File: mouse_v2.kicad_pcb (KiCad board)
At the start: 2 copper layers, 46.4 x 63 mm, 110 parts, among them J1 DEBUGGER, J10 ENC_MASTER, J11 ENC_SLAVE, J12 MOTOR1, J13 MOTOR2, J14 BATT, J15 DEBUGGER_CONN, J16 JLink_Conn, J2 TOF_MASTER, J3 TOF_SLAVE, J4 TOF_MASTER, J5 TOF_SLAVE, J6 TOF_MASTER, J7 TOF_SLAVE, J8 ENC_MASTER, J9 ENC_SLAVE, Q1 IRFML8244, Q2 IRLML6402, Q3 IRFML8244, Q4 IRFML8244, SW1 RESET_SW, SW2 BATTERY_SW, SW3 USER_SW, U1 STM32F413C, U10 AD8602D, U11 TPS62203DBV, U12 TPS62200DBV, U2 VL6180X, U3 VL6180X, U4 VL6180X, U5 MA702GQ, U6 MA702GQ, U7 DRV8835, U8 ICM20648, U9 NJM2732

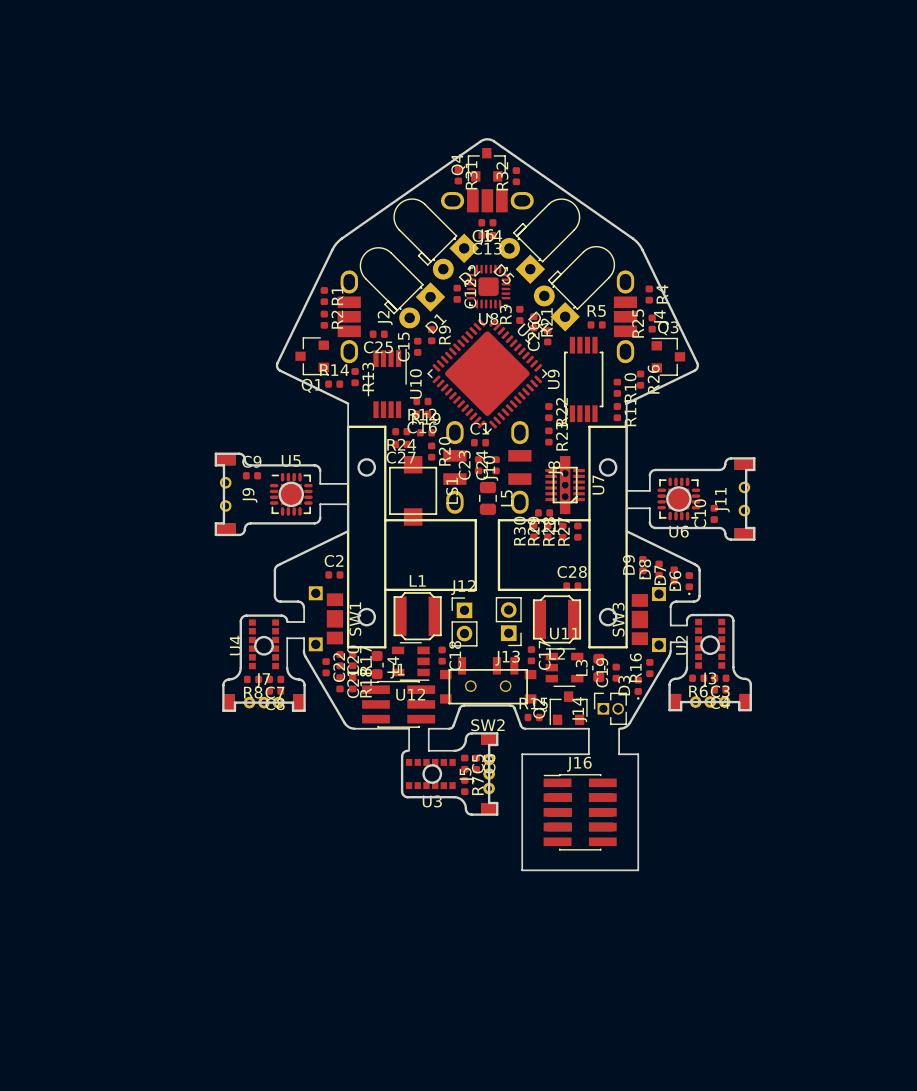
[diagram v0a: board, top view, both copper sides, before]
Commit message: [add] Finished to manual routing.
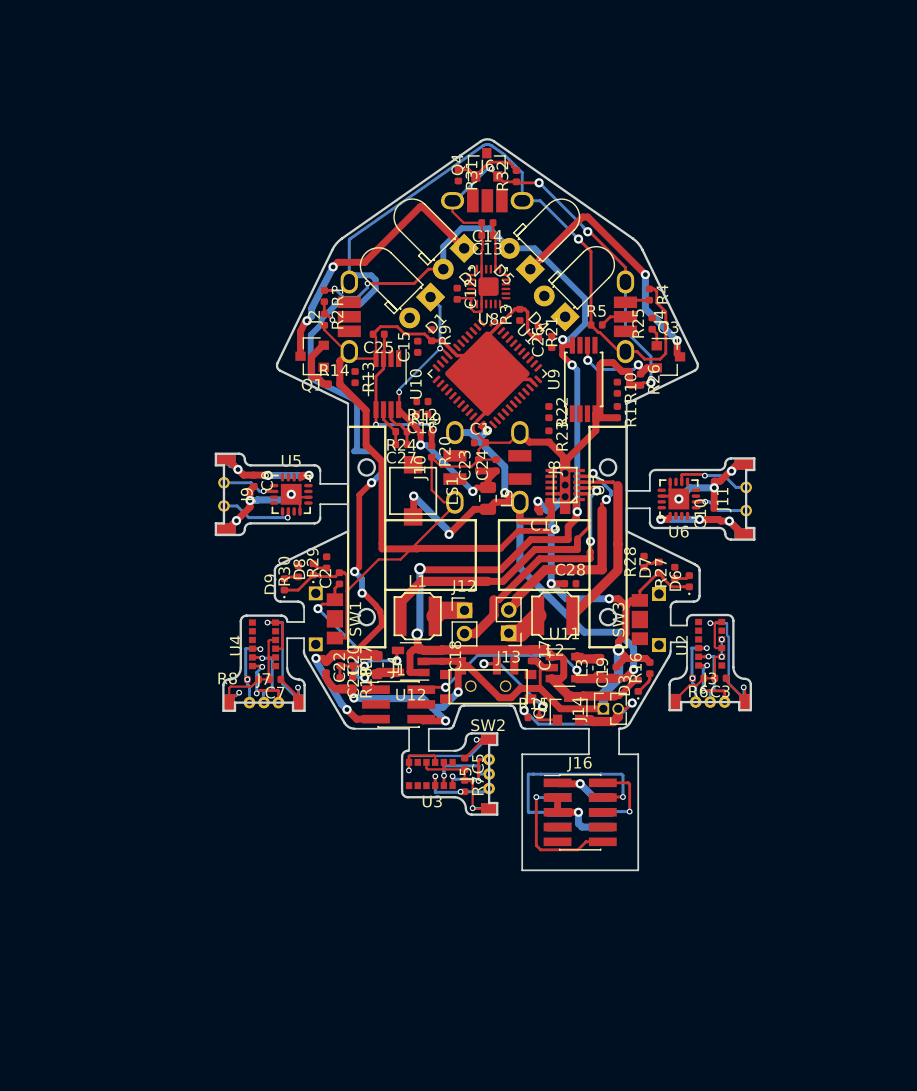
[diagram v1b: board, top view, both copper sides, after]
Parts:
- removed C4, C6, C8: 100n, Capacitor_SMD:C_0402_1005Metric
- moved D9 30.9 mm to (133.8, 119.7)
- moved D8 29.8 mm to (136.3, 118.4)
- moved R30 20.6 mm to (135.0, 118.5)
- moved R29 19.2 mm to (137.4, 117.8)
- moved R27 9.07 mm to (167.4, 118.7)
- moved R28 7.47 mm to (164.8, 117.7)
- moved D7 1.46 mm to (166.1, 118.2)
- moved R21 0.92 mm to (155.7, 97.9)
- moved C26 0.59 mm to (156.8, 98.8)
- moved C2 0.52 mm to (138.5, 119.1), turned to 90 degrees
- moved C9 0.46 mm to (131.2, 110.7), turned to 270 degrees
- moved L2 0.36 mm to (157.1, 122.4)
- moved C28 0.26 mm to (158.4, 119.6)
- moved C11 0.16 mm to (156.3, 113.4)
- moved J11 0.15 mm to (173.6, 112.3)
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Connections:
- net Net-(J15-Pad2) renamed /converter/3.3V
- net Net-(J15-Pad6) renamed /converter/t_GND
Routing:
- net GND: track 0.00 -> 275.3 mm, vias 0 -> 12
- net 2.8V: track 0.00 -> 112.5 mm, vias 0 -> 6
- net BATT: track 0.00 -> 103.0 mm, vias 0 -> 7
- net 3.3V: track 0.00 -> 76.2 mm, vias 0 -> 7
- net 3.3VA: track 0.00 -> 27.2 mm, vias 0 -> 4
- net Net-(L1-Pad2): track 0.00 -> 24.6 mm
- net Net-(D2-Pad1): track 0.00 -> 23.5 mm, vias 0 -> 2
- net Net-(J12-Pad2): track 0.00 -> 22.2 mm, vias 0 -> 2
- net Net-(D5-Pad1): track 0.00 -> 22.2 mm, vias 0 -> 2
- net Net-(J13-Pad2): track 0.00 -> 20.5 mm, vias 0 -> 2
- net /converter/SWCLK: track 0.00 -> 18.5 mm, vias 0 -> 1
- net /ToF3/t_GND: track 0.00 -> 18.3 mm, vias 0 -> 2
- net /ToF1/t_GND: track 0.00 -> 18.0 mm, vias 0 -> 2
- net /ToF2/t_GND: track 0.00 -> 17.8 mm, vias 0 -> 2
- net Net-(J14-Pad2): track 0.00 -> 17.0 mm, vias 0 -> 2
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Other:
- outline, holes or cut-outs redrawn
- net class Default: via_dia 0.8 -> 0.5; via_drill 0.4 -> 0.3
- net class Power added: clearance 0.2, trace_width 0.6, via_dia 0.8, via_drill 0.4

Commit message: [add] Completed routing.
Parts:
- removed D9: LED4, LED_SMD:LED_0402_1005Metric
- removed R30: 1k, Resistor_SMD:R_0402_1005Metric
- moved D6 31.9 mm to (136.8, 118.0)
- moved D7 30.7 mm to (135.4, 118.7)
- moved R28 21.8 mm to (143.2, 114.8)
- moved R27 16.7 mm to (151.1, 115.2)
- moved D8 2.47 mm to (134.0, 119.4)
- moved R29 1.49 mm to (138.6, 116.8)
- moved R9 0.40 mm to (146.4, 98.6)
- moved R12 0.19 mm to (145.5, 103.9)
- moved R21 0.10 mm to (155.8, 97.9)
- renumbered SW2 to ?, J16 to ?, SW1 to ?, U2 to ?, U3 to ?, U4 to ?, U5 to ?, U6 to ?, U8 to ?, J2 to ?, J4 to ?, SW3 to ?, J6 to ?, J8 to ?, J10 to ?, J9 to ?, J11 to ?, U1 to ?, J3 to ?, J5 to ?, J7 to ?, J12 to ?, J13 to ?, J15 to ?
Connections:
- ? pad 10: /MCU/ENC1_A -> /MCU/ENC1_B
- ? pad 11: /MCU/ENC1_B -> /MCU/ENC1_A
- ? pad 18: /MCU/LED1 -> Net-(U1-Pad18)
- ? pad 20: /MCU/LED3 -> Net-(U1-Pad20)
- ? pad 21: /MCU/LED4 -> Net-(U1-Pad21)
- ? pad 25: /MCU/TOF3_EN -> /MCU/LED1
- ? pad 26: /MCU/TOF2_EN -> /MCU/LED3
- ? pad 27: /MCU/TOF1_EN -> Net-(U1-Pad27)
- ? pad 38: /MCU/IMU_NSS -> /MCU/TOF2_EN
- ? pad 4: Net-(U1-Pad4) -> /MCU/IMU_NSS
- ? pad 43: Net-(U1-Pad43) -> /MCU/TOF3_EN
- ? pad 6: Net-(U1-Pad6) -> /MCU/TOF1_EN
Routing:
- net /MCU/SWDIO: track 0.00 -> 57.4 mm, vias 0 -> 4
- net /MCU/SWCLK: track 0.00 -> 54.1 mm, vias 0 -> 4
- net /MCU/TOF_SDA: track 2.12 -> 55.8 mm, vias 0 -> 9
- net Net-(C26-Pad1): track 3.43 -> 55.7 mm, vias 0 -> 6
- net /MCU/TOF_SCL: track 2.29 -> 50.1 mm, vias 0 -> 5
- net 3.3V: track 76.2 -> 111.0 mm, vias 7 -> 12
- net /MCU/BUTTON: track 0.00 -> 34.7 mm, vias 0 -> 10
- net Net-(LS1-Pad2): track 0.00 -> 33.5 mm, vias 0 -> 4
- net /MCU/NRST: track 12.7 -> 46.1 mm, vias 2 -> 6
- net Net-(R13-Pad2): track 0.00 -> 32.7 mm, vias 0 -> 4
- net Net-(Q1-Pad2): track 4.84 -> 37.2 mm, vias 0 -> 8
- net /MCU/LED3: track 0.00 -> 30.2 mm, vias 0 -> 2
- net /MCU/SPEAKER: track 0.00 -> 26.3 mm, vias 0 -> 6
- net /MCU/TOF3_EN: track 0.00 -> 21.3 mm, vias 0 -> 6
- net /MCU/TOF1_EN: track 0.00 -> 16.5 mm, vias 0 -> 4
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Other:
- net class Default: clearance 0.2 -> 0.14; trace_width 0.25 -> 0.2; via_dia 0.5 -> 0.4
- net class Power: clearance 0.2 -> 0.14; via_dia 0.8 -> 0.4; via_drill 0.4 -> 0.3
- rule trace_clearance: 0.2 -> 0.14
- rule trace_min: 0.2 -> 0.152

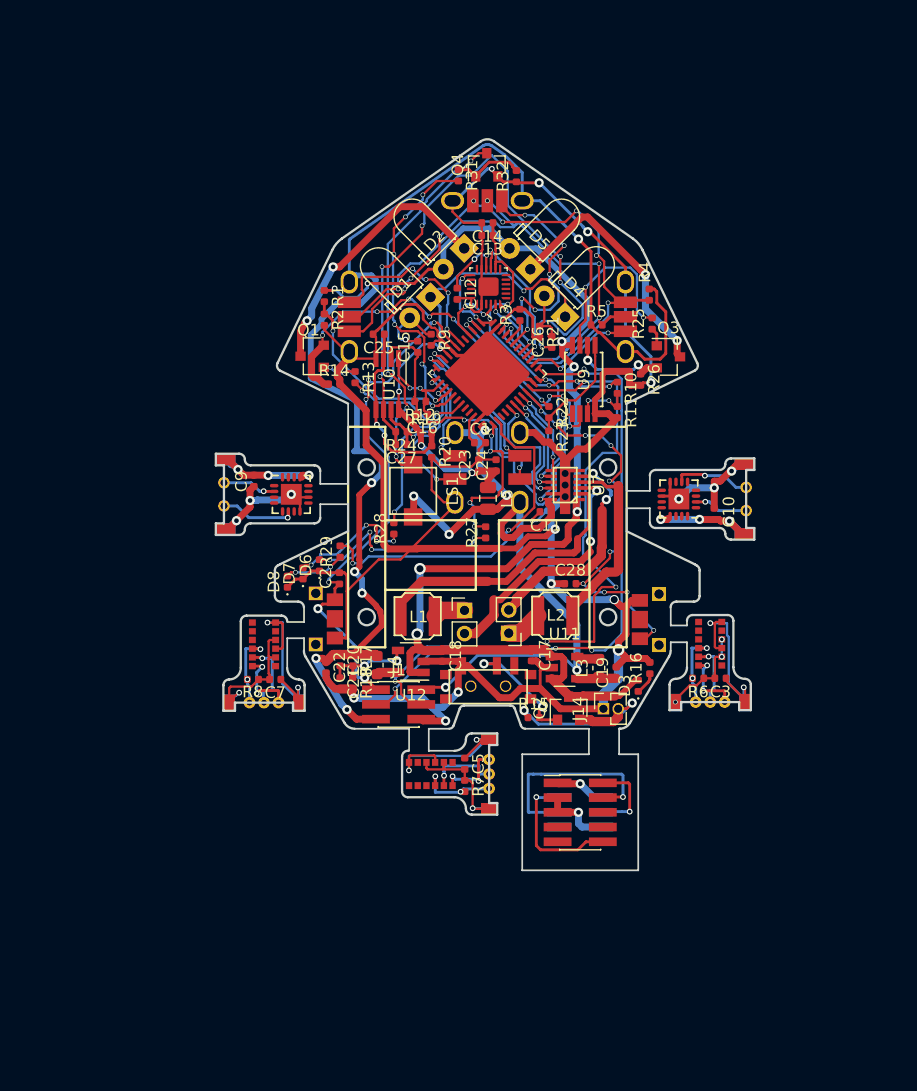
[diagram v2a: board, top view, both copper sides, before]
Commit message: [add] Finished to organize silks.
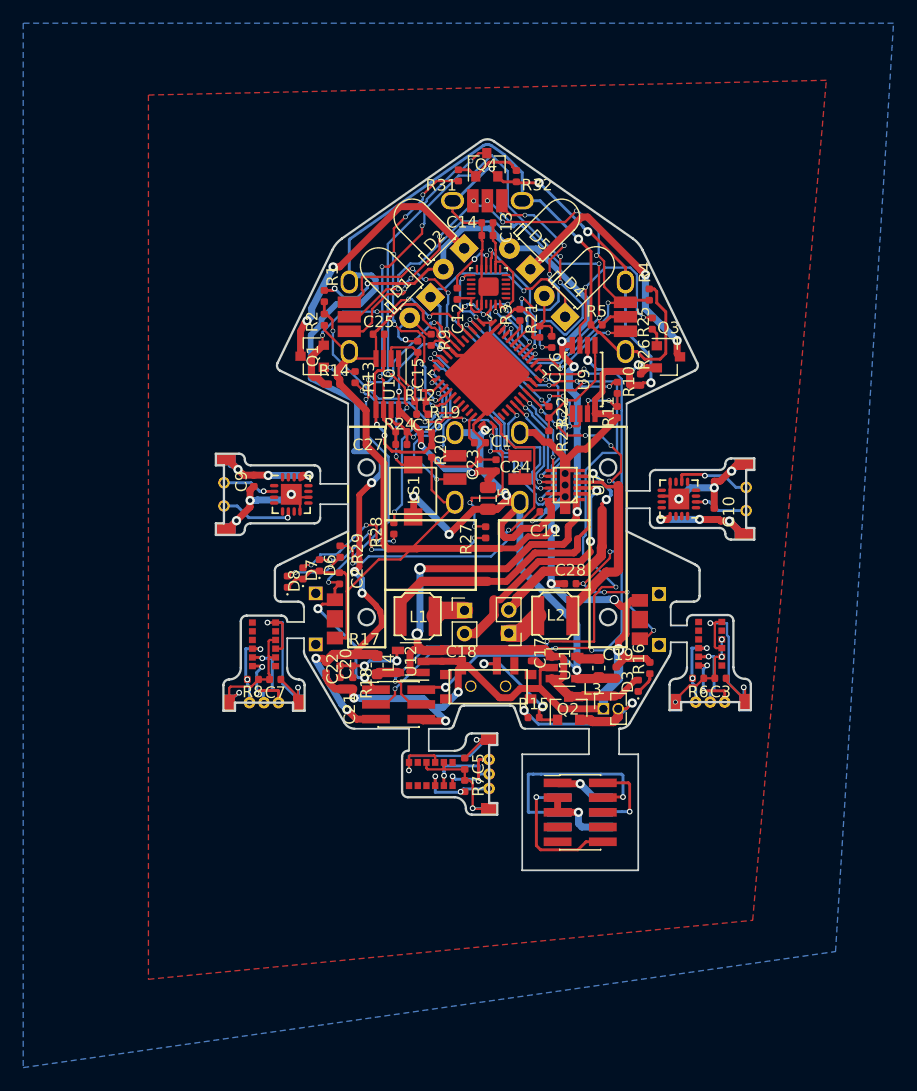
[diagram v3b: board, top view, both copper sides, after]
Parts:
- renumbered J14 to ?, J1 to ?
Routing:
- added copper zone on B.Cu, net GND
- added copper zone on F.Cu, net GND
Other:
- board text added: "2019/05/10"
- board text added: "iimuro"

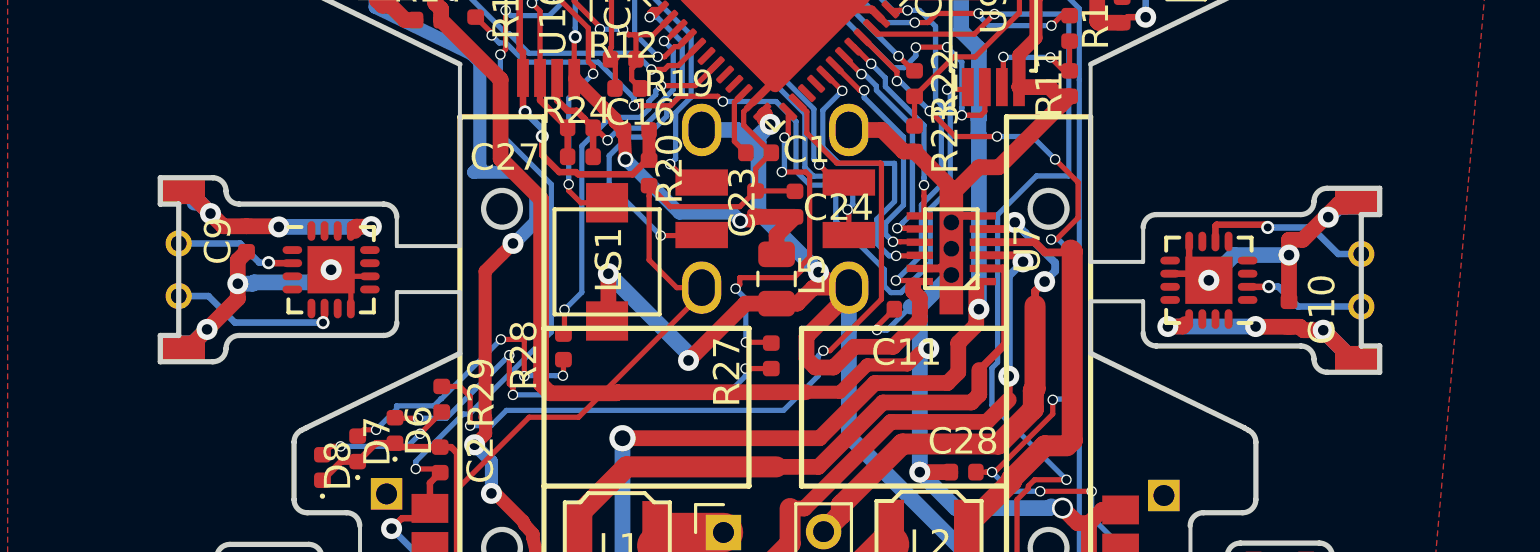
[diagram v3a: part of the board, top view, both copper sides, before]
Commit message: [update] Modified height of encoder board.
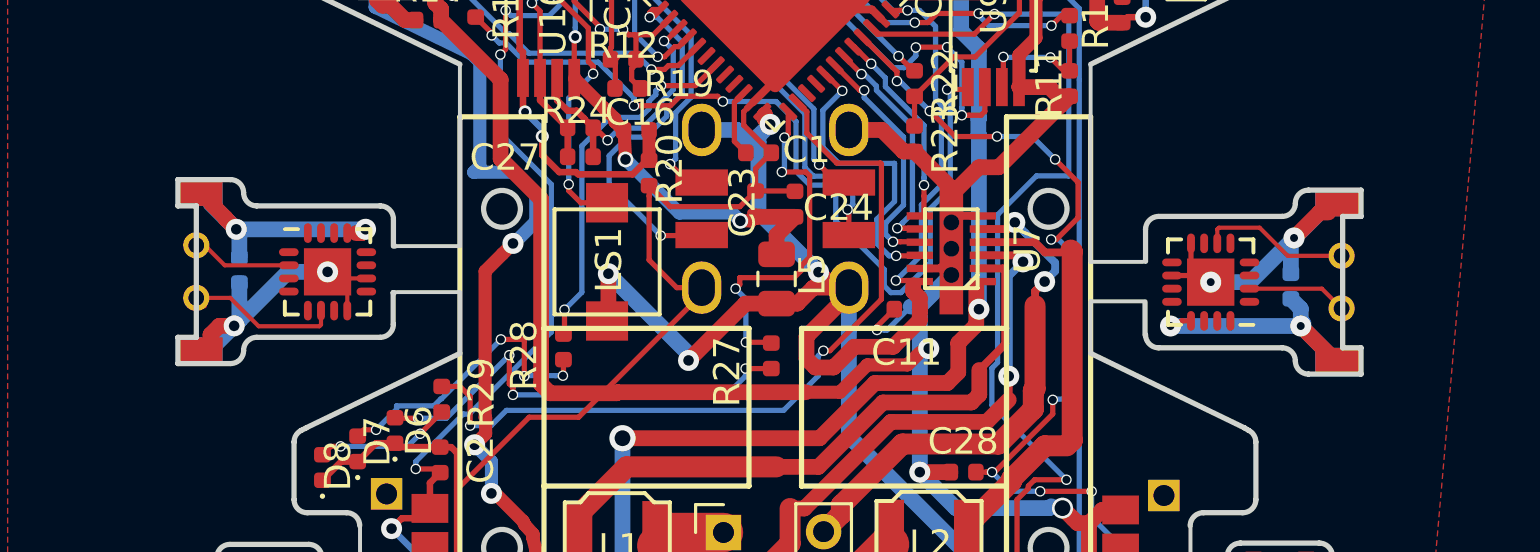
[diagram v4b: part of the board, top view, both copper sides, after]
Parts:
- added G***: LOGO, logos:rust_logo, B.Cu at (159.6, 126.7)
- added G***: LOGO, logos:pomu, B.Cu at (151.4, 100.5)
- C10, C9: moved to B.Cu
- moved C9 1.22 mm to (130.9, 111.9)
- moved C10 1.07 mm to (170.9, 112.5)
- moved ? 0.75 mm to (172.8, 112.4)
- moved ? 0.67 mm to (129.2, 112.0)
- moved ? 0.16 mm to (134.2, 112.0)
- moved ? 0.10 mm to (167.8, 112.4)
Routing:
- net /encoder2/3V3: track 9.50 -> 10.8 mm, vias 3 -> 2
- net /encoder1/3V3: track 8.74 -> 9.59 mm, vias 3 -> 2
- net Net-(J11-Pad2): track 4.22 -> 3.42 mm, vias 1 -> 0
- net Net-(J11-Pad3): track 6.20 -> 5.45 mm, vias 1 -> 0
- net Net-(J9-Pad2): track 4.21 -> 3.51 mm, vias 1 -> 0
- net /encoder2/t_GND: track 13.0 -> 12.4 mm, vias 3 -> 2
- net Net-(J9-Pad3): track 6.15 -> 5.75 mm, vias 1 -> 0
- net /encoder1/t_GND: track 12.5 -> 12.4 mm, vias 3 -> 2
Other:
- board size 46.4 x 63 mm -> 45.5 x 63 mm
- net class Default: trace_width 0.2 -> 0.16
- net class Power: via_dia 0.4 -> 0.8; via_drill 0.3 -> 0.4
- board text added: "2019/10/10"
- board text removed: "2019/05/10"
